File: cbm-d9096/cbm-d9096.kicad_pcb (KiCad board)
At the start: 2 copper layers, 90.2 x 68.6 mm, 33 parts, among them J1 IEEE488 Header, J2 LED, J3 SD CARD, J4 WP/CD Jumper, J5 SD CARD, J6 WP/CD Jumper, J7 RESET, J8 Alt PWR, J9 Barrel_Jack, U1 ATmega1284-P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

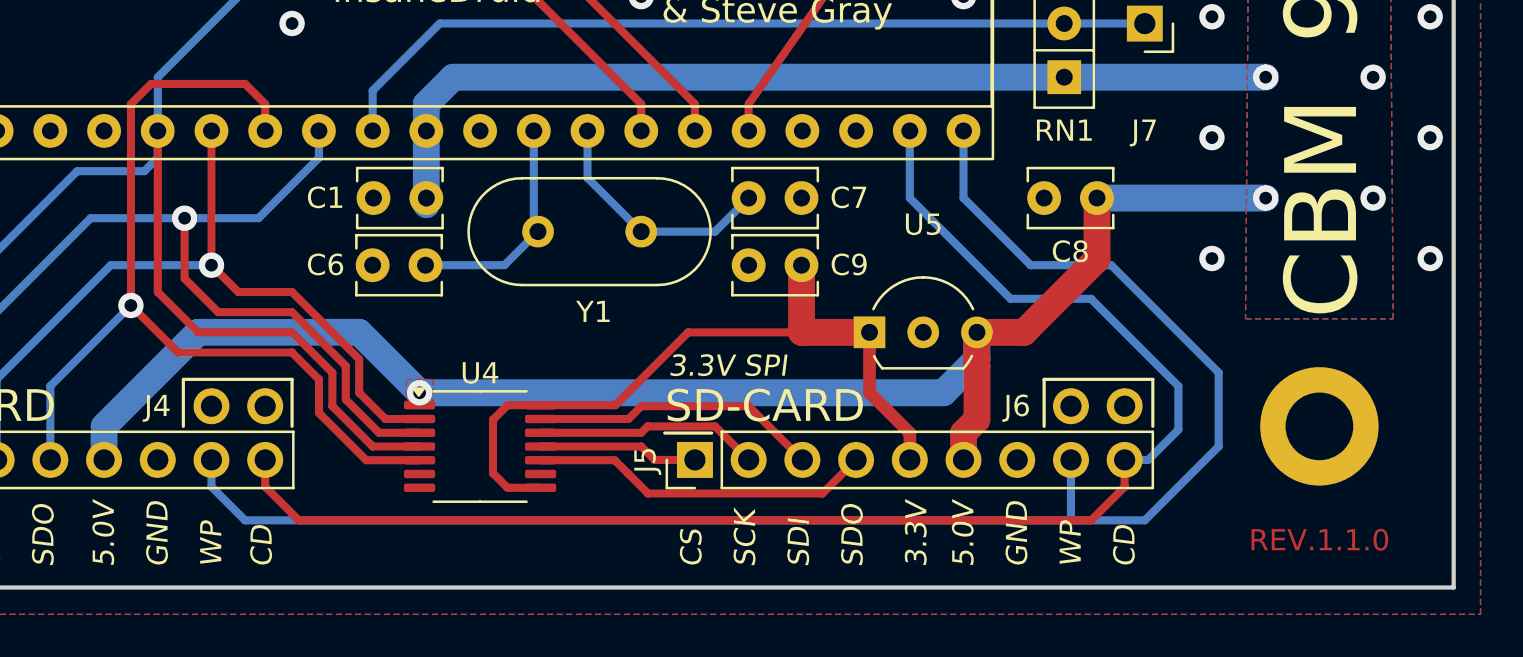
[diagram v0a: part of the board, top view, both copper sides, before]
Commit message: added jumper to quickly enable/disable the level shifter
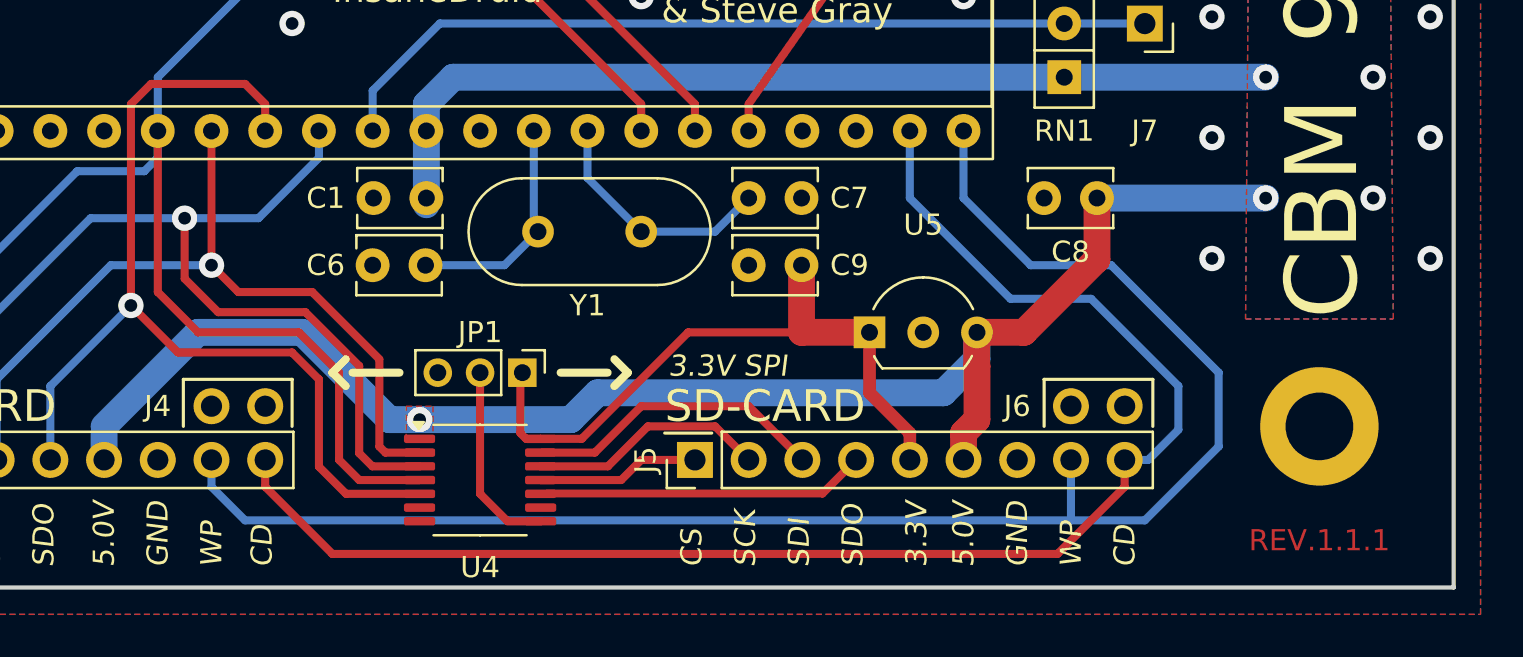
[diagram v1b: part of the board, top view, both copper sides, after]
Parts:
- added JP1: 3.3V port enable/disable, Connector_PinHeader_2.00mm:PinHeader_1x03_P2.00mm_Vertical, F.Cu at (161.7, 124.5)
- moved U4 1.59 mm to (159.7, 129.5)
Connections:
- U4 pad 8: +3.3V -> Net-(JP1-C)
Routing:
- net Net-(JP1-C): track 0.00 -> 9.13 mm
- net +3.3V: track 34.5 -> 31.5 mm
- net /SCLK_{SPI}: track 45.5 -> 47.6 mm
- net /SDO_{SPI}: track 44.4 -> 46.6 mm
- net /SDI_{SPI}: track 36.3 -> 38.5 mm
- net /CS_{SPI}: track 94.8 -> 96.9 mm
- net CD_{SPI}: track 69.2 -> 70.6 mm
- net +5V: track 220.1 -> 221.1 mm
- net /SDO_{BUFF}: track 16.2 -> 15.3 mm
- net /SDI_{BUFF}: track 13.7 -> 14.3 mm
- net /SCLK_{BUFF}: track 10.6 -> 11.3 mm
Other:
- board text added: "REV.1.1.1"
- board text removed: "REV.1.1.0"
